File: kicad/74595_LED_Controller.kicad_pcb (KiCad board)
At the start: 2 copper layers, 12 parts, among them P1 CONN_5, P2 CONN_5, P3 CONN_9, U1 74HC595

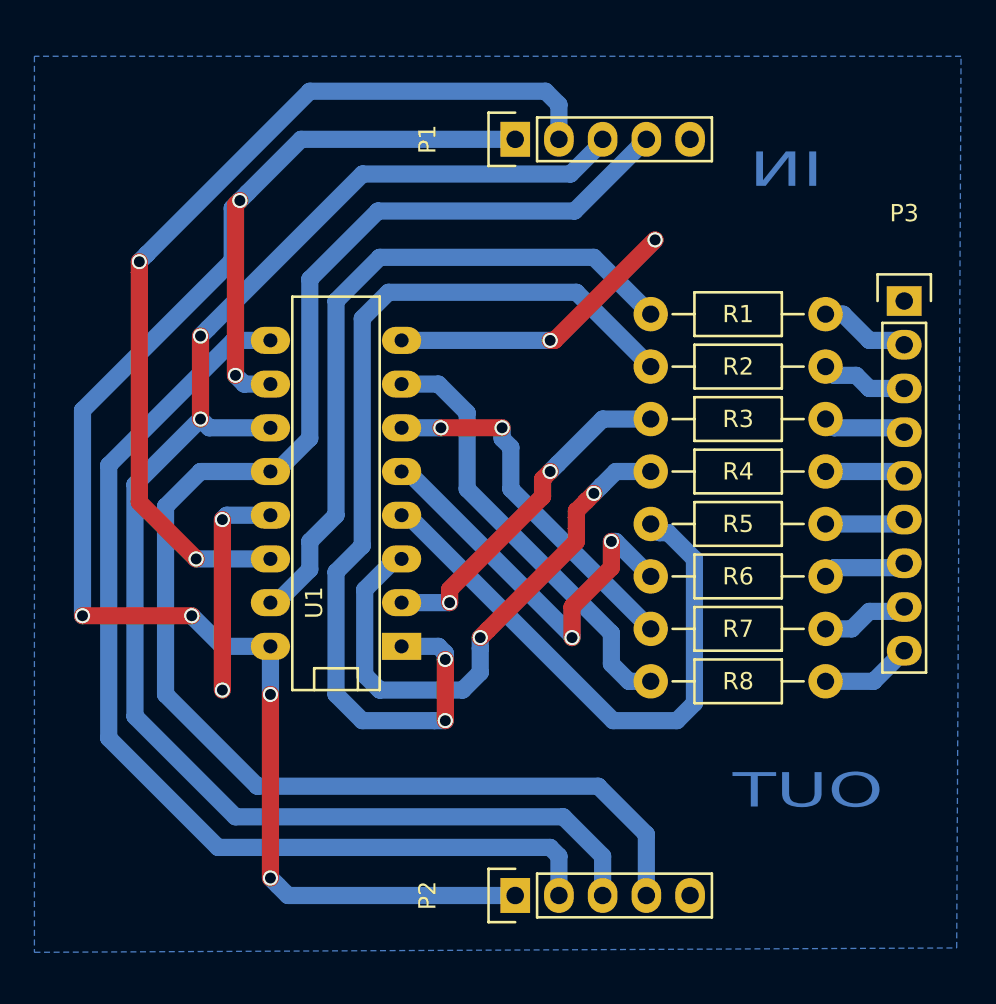
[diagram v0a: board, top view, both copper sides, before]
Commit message: Added a filtering ceramic capacitor between the power supply pins for the 74595 IC.
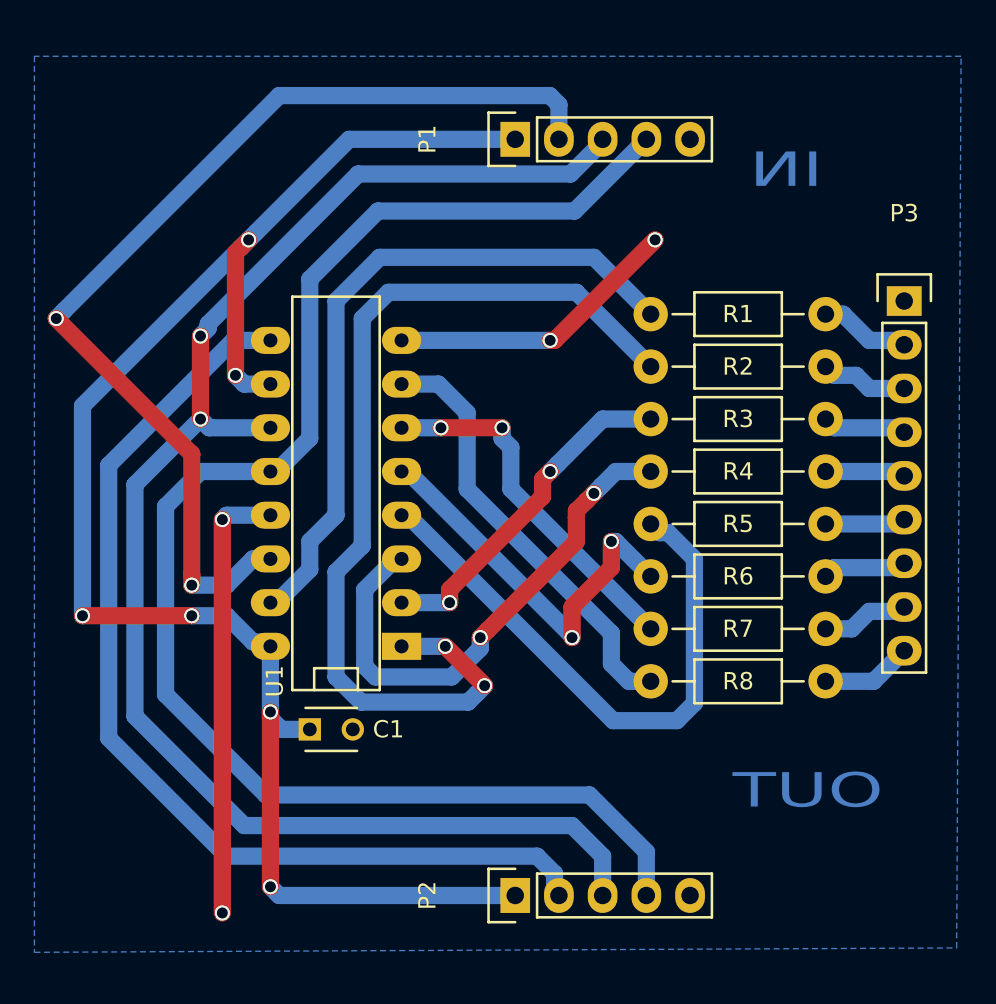
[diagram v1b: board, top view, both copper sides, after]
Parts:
- added C1: C, Capacitors_ThroughHole:C_Disc_D3_P2.5, F.Cu at (118.6, 166.4)
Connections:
- net VCC renamed +5V
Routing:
- net GND: track 30.0 -> 42.9 mm
- net SERIAL_DATA_INPUT: track 53.8 -> 60.8 mm
- net Net-(R4-Pad2): track 33.3 -> 31.6 mm
- net Net-(R2-Pad2): track 55.3 -> 56.1 mm
- net SERIAL_DATA_OUTPUT: track 59.6 -> 58.8 mm
- net REGISTER_CLOCK: track 88.0 -> 87.4 mm

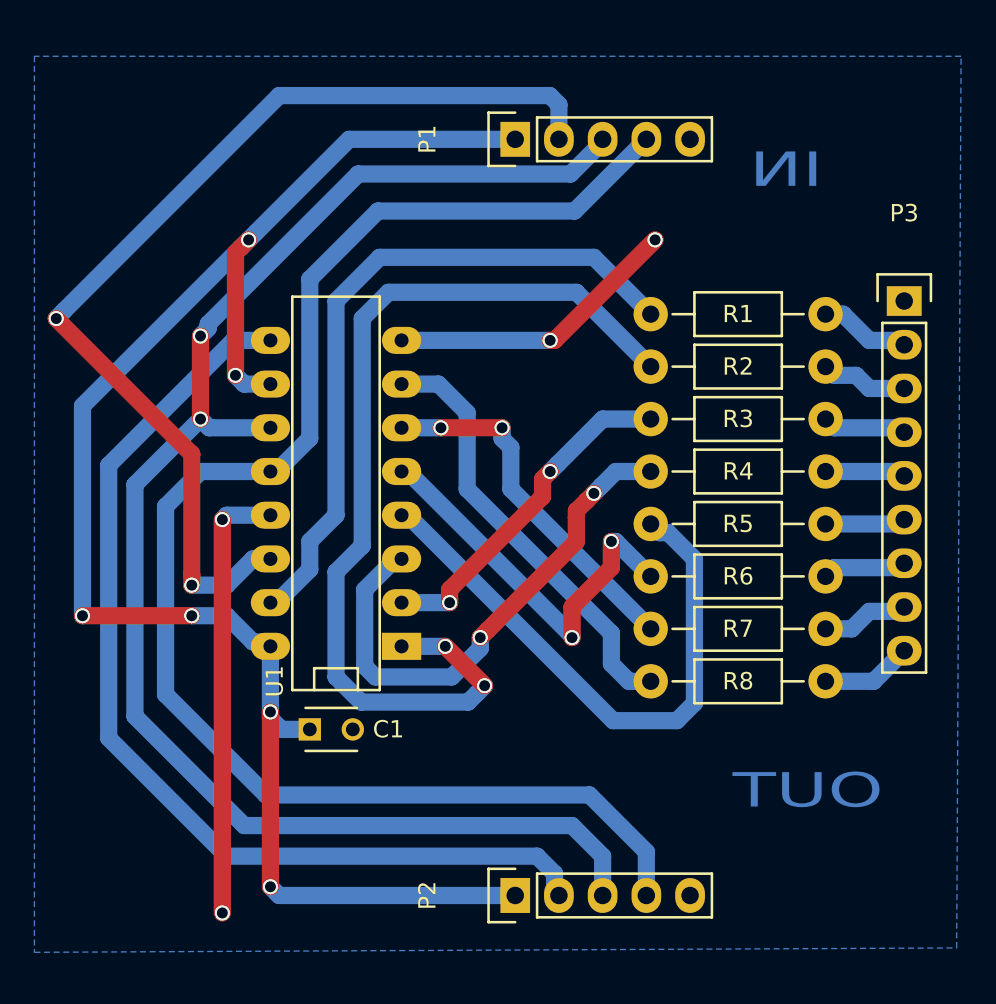
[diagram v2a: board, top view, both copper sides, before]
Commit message: pcb edge cuts (with mount holes in the 4 corners)
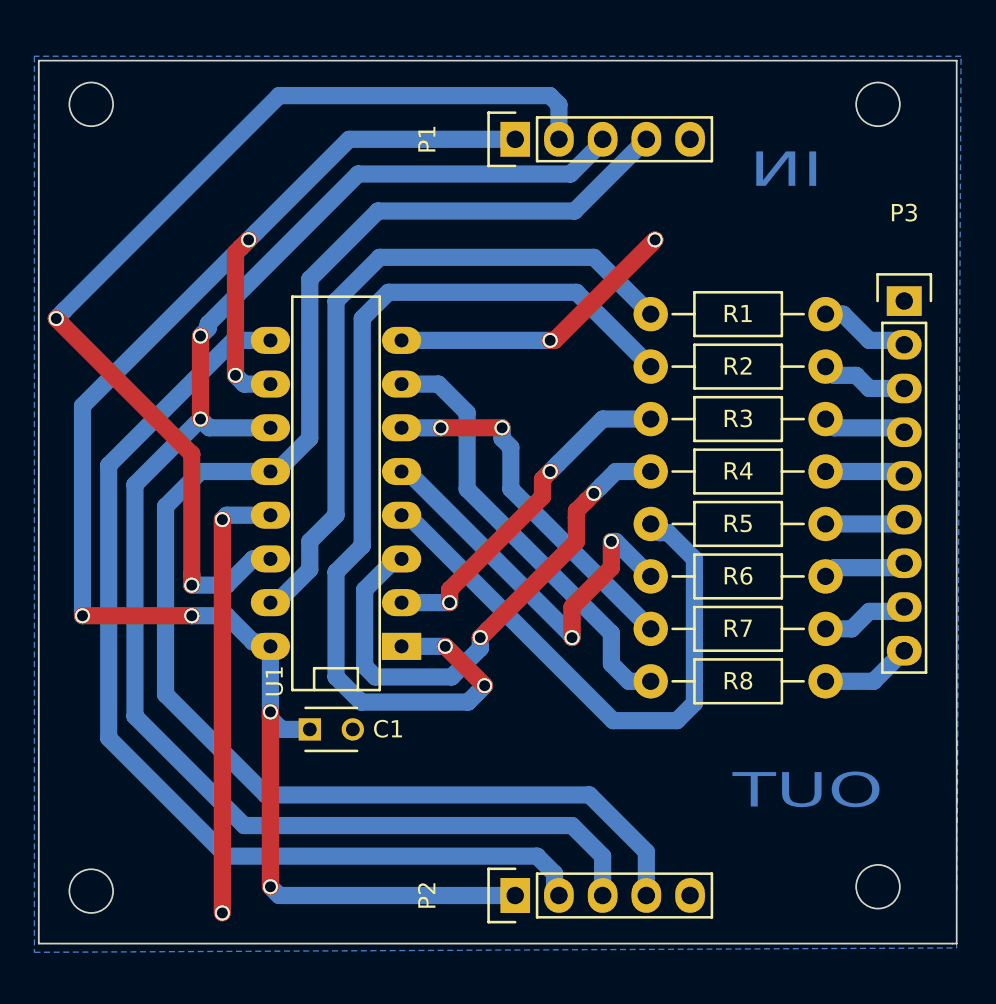
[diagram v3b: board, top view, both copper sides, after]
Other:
- board outline added: 53.3 x 51.3 mm
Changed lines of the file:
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@@
     (links 31)
     (no_connects 0)
-    (area 102.616 127.254 156.464001 179.324001)
+    (area 102.819999 127.457999 156.260001 178.866001)
     (thickness 1.6)
-    (drawings 2)
+    (drawings 11)
     (tracks 203)
     (zones 0)
@@
     )
   )
+  (gr_circle (center 105.918 175.768) (end 107.188 175.768) (layer Edge.Cuts) (width 0.1))
+  (gr_circle (center 105.918 130.048) (end 107.188 130.048) (layer Edge.Cuts) (width 0.1))
+  (gr_circle (center 151.638 130.048) (end 152.908 130.048) (layer Edge.Cuts) (width 0.1))
+  (gr_line (start 156.21 178.816) (end 155.956 178.816) (layer Edge.Cuts) (width 0.1))
+  (gr_line (start 156.21 127.508) (end 156.21 178.816) (layer Edge.Cuts) (width 0.1))
+  (gr_line (start 102.87 127.508) (end 156.21 127.508) (layer Edge.Cuts) (width 0.1))
+  (gr_line (start 102.87 178.816) (end 102.87 127.508) (layer Edge.Cuts) (width 0.1))
+  (gr_line (start 155.956 178.816) (end 102.87 178.816) (layer Edge.Cuts) (width 0.1))
+  (gr_circle (center 151.638 175.514) (end 152.4 176.53) (layer Edge.Cuts) (width 0.1))
   (gr_text IN (at 146.304 133.858) (layer B.Cu)
     (effects (font (size 2 3) (thickness 0.5)) (justify mirror))

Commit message: melhorando o layout e a camada de silk (adicionando labels com os nomes dos sinais de cada pino).
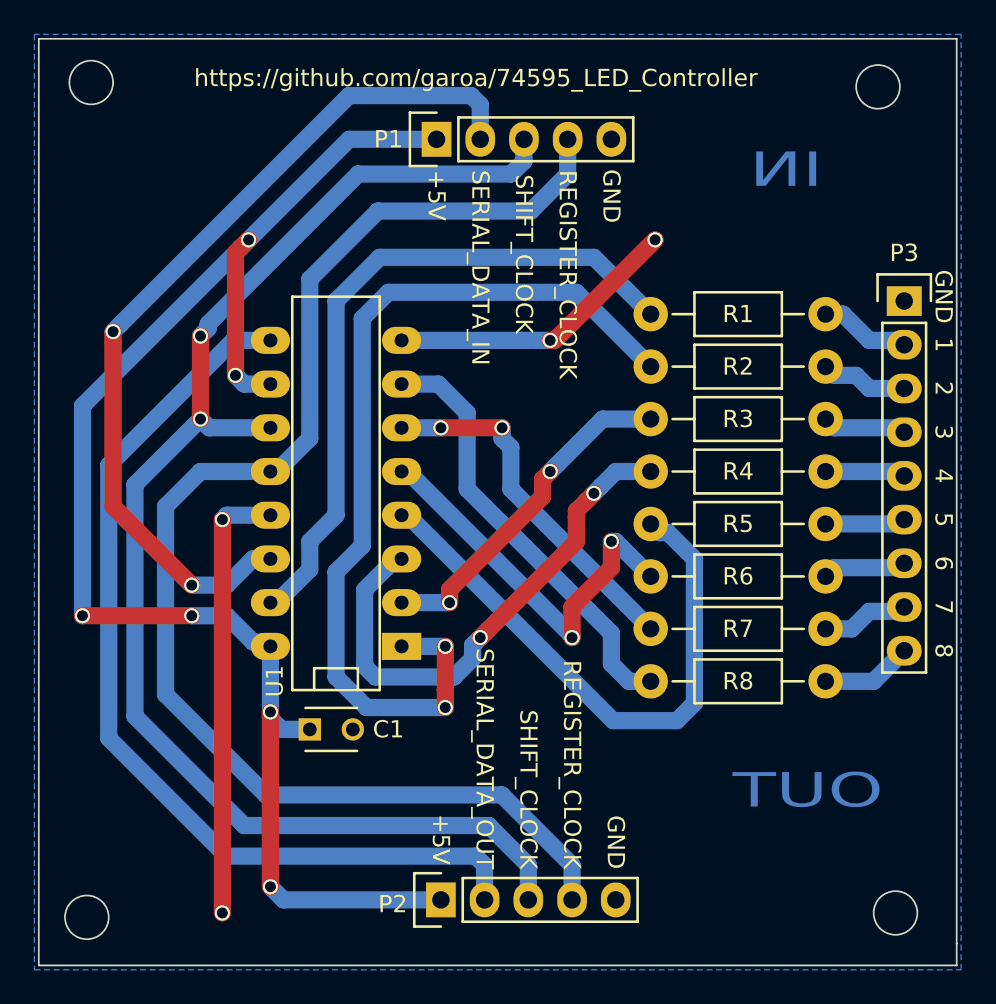
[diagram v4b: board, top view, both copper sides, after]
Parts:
- moved P1 4.57 mm to (126.0, 132.1)
- moved P2 4.33 mm to (126.2, 176.3)
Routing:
- net SERIAL_DATA_INPUT: track 60.8 -> 51.1 mm
- net +5V: track 97.2 -> 88.4 mm
- net SHIFT_CLOCK: track 89.1 -> 80.8 mm
- net REGISTER_CLOCK: track 87.4 -> 79.5 mm
- net SERIAL_DATA_OUTPUT: track 58.8 -> 55.2 mm
- net Net-(R2-Pad2): track 56.1 -> 53.8 mm
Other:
- board size 53.3 x 51.3 mm -> 53.3 x 53.8 mm
- board text added: "+5V"
- board text added: "1"
- board text added: "2"
- board text added: "3"
- board text added: "4"
- board text added: "5"
- board text added: "6"
- board text added: "7"
- board text added: "8"
- board text added: "GND"
- board text added: "REGISTER_CLOCK"
- board text added: "SERIAL_DATA_IN"
- board text added: "SERIAL_DATA_OUT"
- board text added: "SHIFT_CLOCK"
- board text added: "https://github.com/garoa/74595_LED_Controller"

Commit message: adicionando segunda camada (opcional)
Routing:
- net GND: vias 4 -> 5
- added copper zone on F.Cu, net GND
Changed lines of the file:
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@@
   (general
     (links 31)
-    (no_connects 1)
+    (no_connects 0)
     (area 102.819999 126.187999 156.260001 180.136001)
     (thickness 1.6)
     (drawings 31)
-    (tracks 202)
+    (tracks 204)
     (zones 0)
     (modules 13)
@@
   (segment (start 122.578969 136.247031) (end 118.618 140.208) (width 1) (layer B.Cu) (net 3))
   (segment (start 116.6876 151.384) (end 116.332 151.384) (width 1) (layer B.Cu) (net 3))
+  (segment (start 113.538 159.004) (end 113.538 163.36403) (width 1) (layer F.Cu) (net 4))
+  (segment (start 113.538 164.084) (end 113.538 163.36403) (width 1) (layer F.Cu) (net 4))
+  (via (at 113.538 163.36403) (size 0.889) (drill 0.635) (layers F.Cu B.Cu) (net 4))
   (segment (start 113.538 164.084) (end 113.538 177.038) (width 1) (layer F.Cu) (net 4))
   (via (at 113.538 177.038) (size 0.889) (drill 0.635) (layers F.Cu B.Cu) (net 4))
-  (segment (start 113.538 159.004) (end 113.538 164.084) (width 1) (layer F.Cu) (net 4))
   (segment (start 113.538 154.178) (end 113.538 159.004) (width 1) (layer F.Cu) (net 4))
   (segment (start 116.332 153.924) (end 113.792 153.924) (width 1) (layer B.Cu) (net 4))
@@
     (min_thickness 0.254)
     (fill yes (arc_segments 16) (thermal_gap 0.508) (thermal_bridge_width 0.508))
+    (polygon
+      (pts
+        (xy 102.616 125.984) (xy 102.616 180.34) (xy 156.464 180.34) (xy 156.464 125.984)
+      )
+    )
+  )
+  (zone (net 4) (net_name GND) (layer F.Cu) (hatch edge 0.508)
+    (connect_pads (clearance 0.508))
+    (min_thickness 0.254)
+    (fill yes (arc_segments 16) (thermal_gap 0.508) (thermal_bridge_width 0.508))

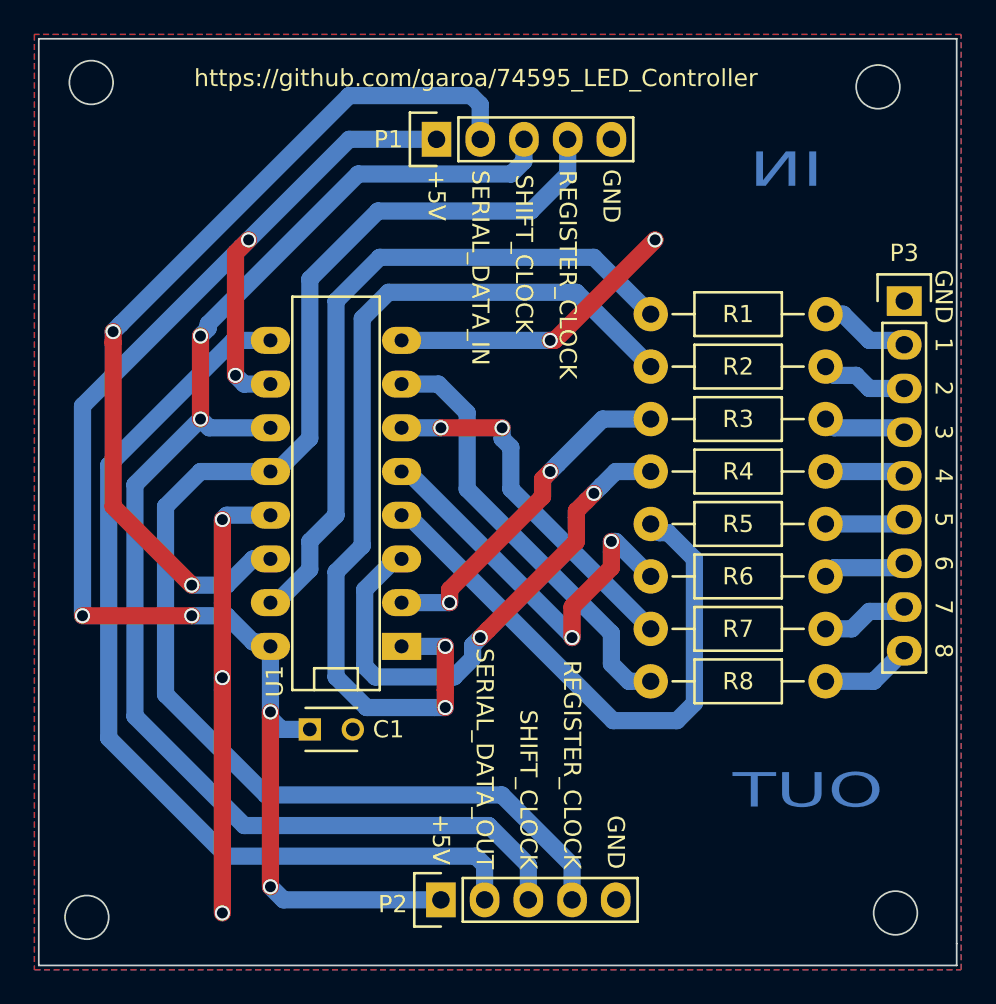
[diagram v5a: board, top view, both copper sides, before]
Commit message: Começando a adaptar a placa para fabricação no http://curtacircuitos.com.br/ Talvez seja bom abrir um branch para manter o projeto de trilhas grossas para fabricação caseira. E deixar o branch principal divergir para uma solução mais compacta e adequada para fabricação profissional...
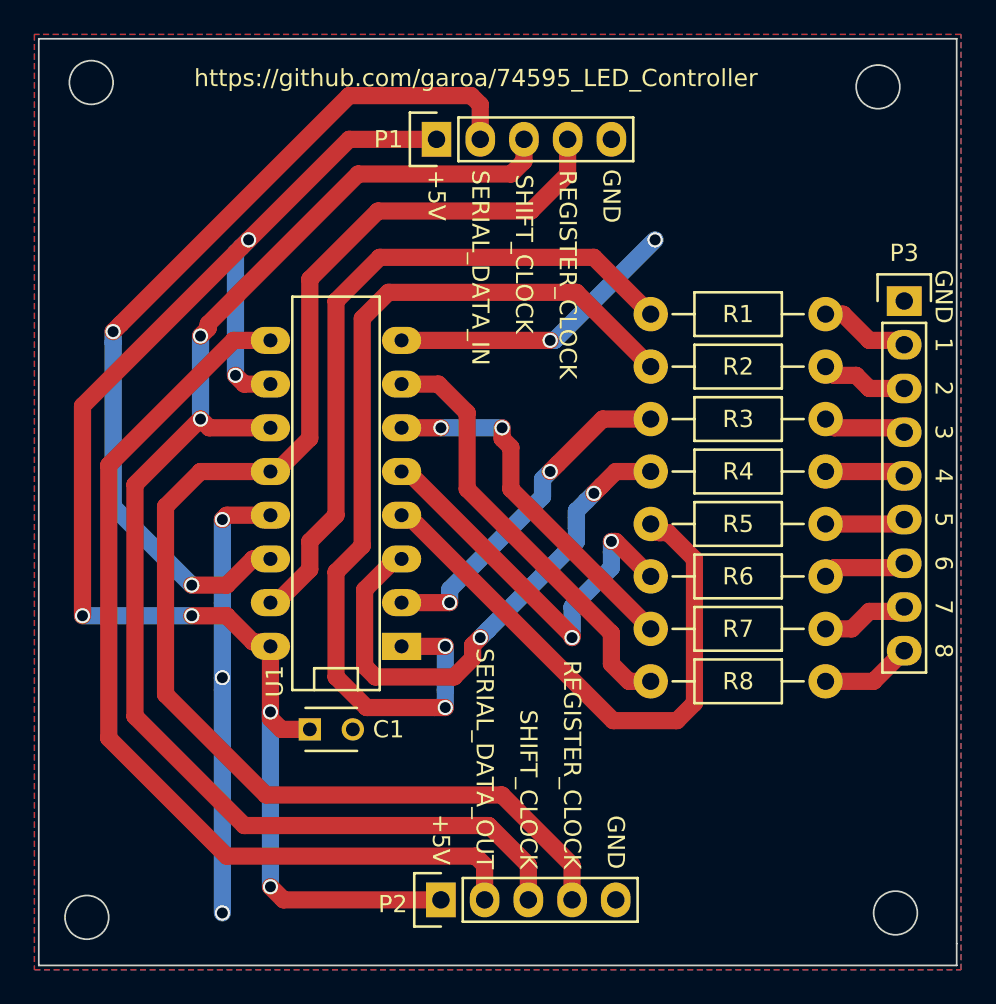
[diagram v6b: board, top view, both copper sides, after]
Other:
- board text removed: "IN"
- board text removed: "OUT"
